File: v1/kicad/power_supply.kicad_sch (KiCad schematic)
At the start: 33 parts, among them J1 Screw_Terminal_01x03, U14 LM7812, U8 LM7815, U9 LM7915

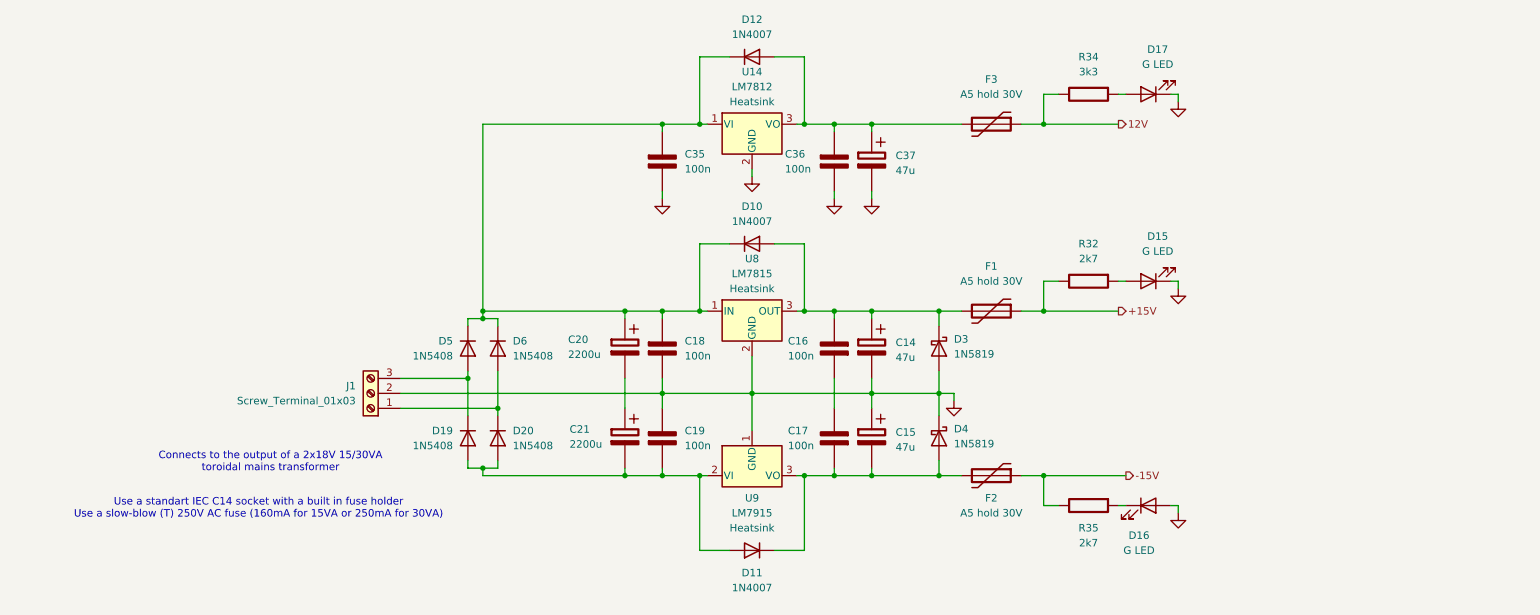
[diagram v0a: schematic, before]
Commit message: Changed the file structure
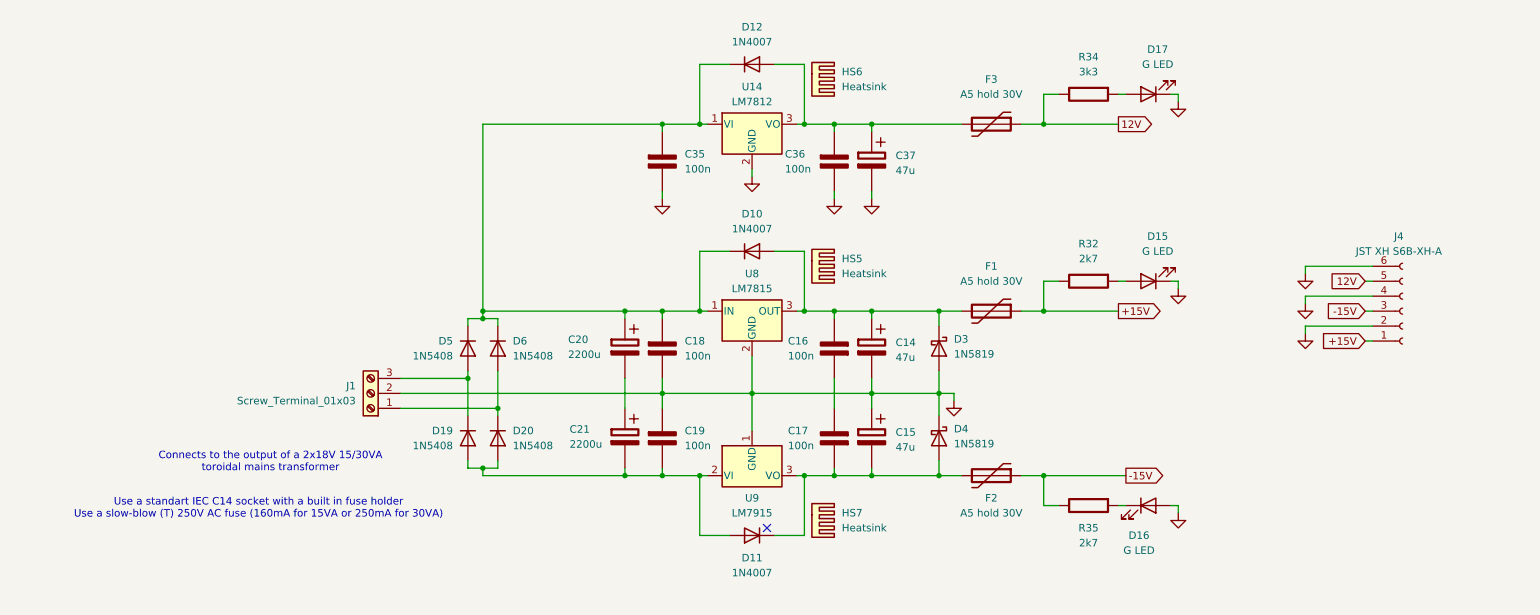
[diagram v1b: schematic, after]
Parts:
- added HS5, HS6, HS7: Heatsink, symbol Mechanical:Heatsink
- added J4: JST XH S6B-XH-A, Connector_JST:JST_XH_S6B-XH-A_1x06_P2.50mm_Horizontal, symbol Connector:Conn_01x06_Socket
- D10, D11, D12: footprint Diode_THT:D_DO-35_SOD27_P7.62mm_Horizontal -> Diode_THT:D_DO-41_SOD81_P10.16mm_Horizontal
- D3, D4: footprint (none) -> Diode_THT:D_DO-41_SOD81_P10.16mm_Horizontal
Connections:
- net +15V: now also J4.1 (Pin_1)
- net -15V: now also J4.3 (Pin_3)
- net 12V: now also J4.5 (Pin_5)
- net GND: now also J4.2 (Pin_2), J4.4 (Pin_4), J4.6 (Pin_6)
- new net: C36., C37., D12.2 (A), F3., U14.3 (VO)
- no-connect marks 0 -> 1
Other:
- moved on the sheet: D10, D11, D12

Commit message: Added a DUT board, changed the output connectors , added test hooks, removed unnecessary switches, added FET support
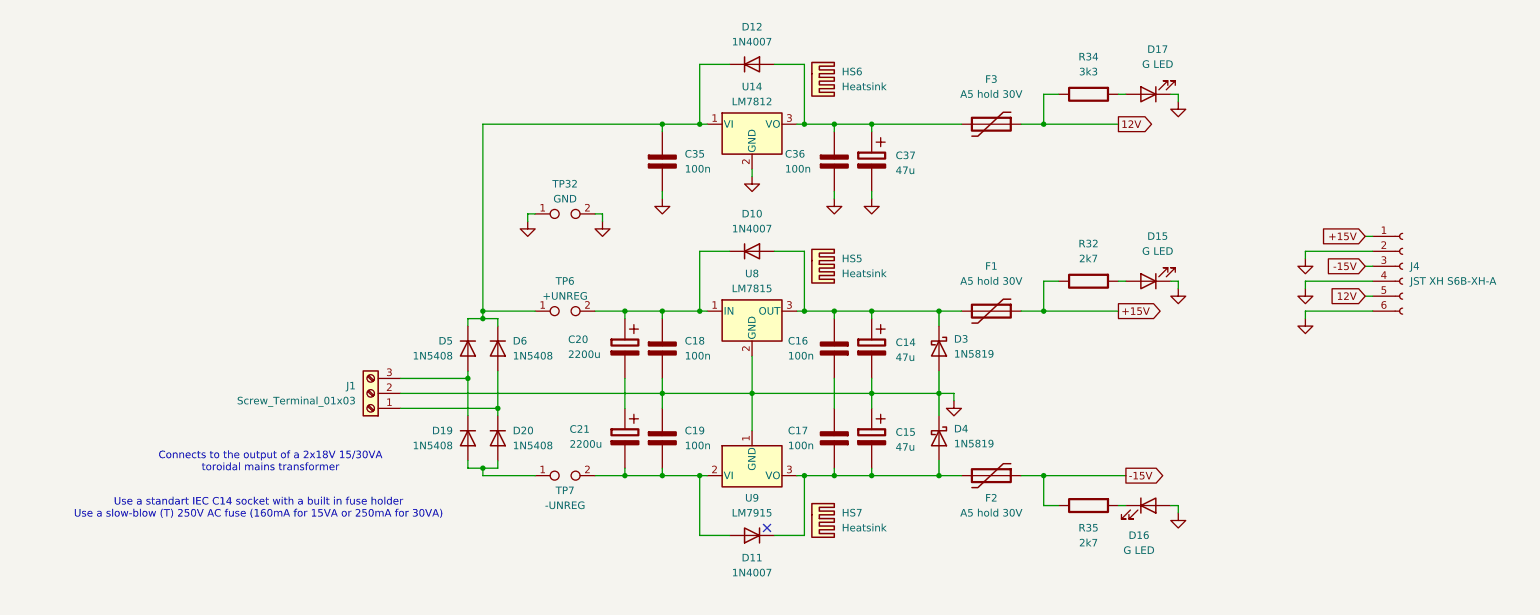
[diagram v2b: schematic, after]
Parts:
- added TP32: GND, symbol Connector:TestPoint_2Pole
- added TP6: +UNREG, symbol Connector:TestPoint_2Pole
- added TP7: -UNREG, symbol Connector:TestPoint_2Pole
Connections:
- net GND: now also TP32.1, TP32.2
- new net: C18., C20., D10.1 (K), TP6.2, U8.1 (IN)
- new net: C19., C21., D11.2 (A), TP7.2, U9.2 (VI)
- new net: D19.2 (A), D20.2 (A), TP7.1
- new net: C36., C37., D12.2 (A), F3., U14.3 (VO)
- new net: C35., D12.1 (K), D5.1 (K), D6.1 (K), TP6.1, U14.1 (VI)
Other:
- moved on the sheet: J4

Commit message: Added power connector
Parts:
- J1: value Screw_Terminal_01x03 -> 1718757
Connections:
- new net: C36., C37., D12.2 (A), F3., U14.3 (VO)
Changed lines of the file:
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@@
 			)
 		)
-		(property "Value" "Screw_Terminal_01x03"
+		(property "Value" "1718757"
 			(at 81.28 100.33 0)
 			(show_name no)

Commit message: Adding KiKit multiboarding
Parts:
- removed J1: 1718757, symbol Connector:Screw_Terminal_01x03
- removed J4: JST XH S6B-XH-A, Connector_JST:JST_XH_S6B-XH-A_1x06_P2.50mm_Horizontal, symbol Connector:Conn_01x06_Socket
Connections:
- net L1: now reaches D19.1 (K), D5.2 (A)
- net L2: now reaches D20.1 (K), D6.2 (A)
- net GND renamed GNDPWR
- new net: C36., C37., D12.2 (A), F3., U14.3 (VO)
- no-connect marks 1 -> 0

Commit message: Fixed mistakes with the polarity of some caps
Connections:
- net GNDPWR: now also C16., C17., C20., C21.
- new net: C36., C37., D12.2 (A), F3., U14.3 (VO)
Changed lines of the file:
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@@
+	)
+	(junction
+		(at 127 99.06)
+		(diameter 0)
+		(color 0 0 0 0)
 	)
 	(junction
@@
 	)
 	(junction
+		(at 162.56 99.06)
+		(diameter 0)
+		(color 0 0 0 0)
+	)
+	(junction
 		(at 168.91 85.09)
 		(diameter 0)
@@
 	(wire
 		(pts
-			(xy 162.56 96.52) (xy 162.56 101.6)
+			(xy 162.56 99.06) (xy 162.56 101.6)
 		)
 		(stroke
@@
 	(wire
 		(pts
+			(xy 127 99.06) (xy 127 101.6)
+		)
+		(stroke
+			(width 0)
+			(type default)
+		)
+	)
+	(wire
+		(pts
 			(xy 168.91 113.03) (xy 180.34 113.03)
 		)
@@
 	(wire
 		(pts
-			(xy 148.59 99.06) (xy 168.91 99.06)
+			(xy 148.59 99.06) (xy 162.56 99.06)
 		)
 		(stroke
@@
 	(wire
 		(pts
+			(xy 127 96.52) (xy 127 99.06)
+		)
+		(stroke
+			(width 0)
+			(type default)
+		)
+	)
+	(wire
+		(pts
 			(xy 102.87 53.34) (xy 102.87 85.09)
 		)
@@
 	(wire
 		(pts
+			(xy 162.56 96.52) (xy 162.56 99.06)
+		)
+		(stroke
+			(width 0)
+			(type default)
+		)
+	)
+	(wire
+		(pts
 			(xy 156.21 113.03) (xy 157.48 113.03)
 		)
@@
 	(wire
 		(pts
+			(xy 127 99.06) (xy 133.35 99.06)
+		)
+		(stroke
+			(width 0)
+			(type default)
+		)
+	)
+	(wire
+		(pts
 			(xy 180.34 99.06) (xy 180.34 102.87)
 		)
@@
 	(wire
 		(pts
-			(xy 127 96.52) (xy 127 101.6)
-		)
-		(stroke
-			(width 0)
-			(type default)
-		)
-	)
-	(wire
-		(pts
 			(xy 152.4 74.93) (xy 157.48 74.93)
 		)
@@
 	(wire
 		(pts
-			(xy 88.9 99.06) (xy 133.35 99.06)
+			(xy 88.9 99.06) (xy 127 99.06)
 		)
 		(stroke
@@
 		)
 		(stroke
+			(width 0)
+			(type default)
+		)
+	)
+	(wire
+		(pts
+			(xy 162.56 99.06) (xy 168.91 99.06)
+		)
+		(stroke

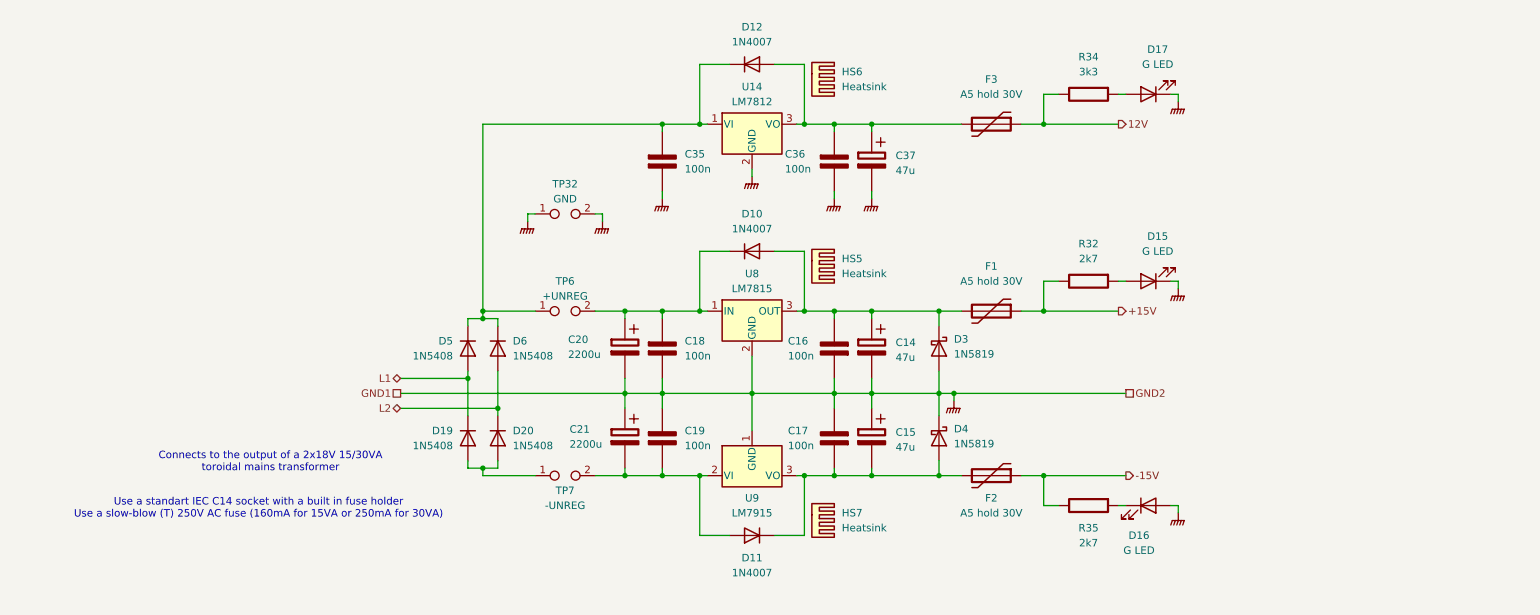
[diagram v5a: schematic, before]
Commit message: Fixed mistakes and made making a BOM easier
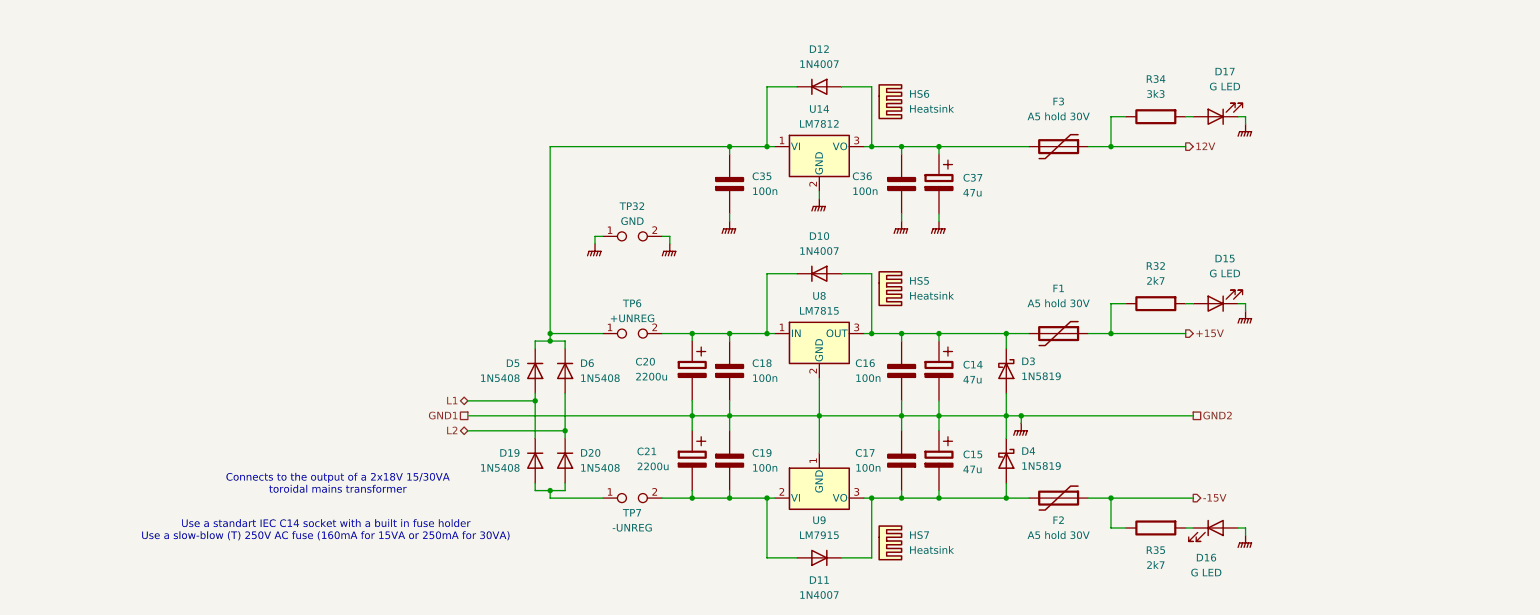
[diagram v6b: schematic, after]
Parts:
- C14, C15, C20, C21, C37: Spend (none) -> $$$
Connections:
- net +15V: now also F1.1, R32.2; no longer F1., R32.
- net -15V: now also F2.1, R35.2; no longer F2., R35.
- net 12V: now also F3.1, R34.2; no longer F3., R34.
- net GNDPWR: now also C14.2, C15.1, C16.1, C17.2, C18.2, C19.1, C20.2, C21.1, C35.2, C36.2, C37.2; no longer C14., C15., C16., C17., C18., C19., C20., C21., C35., C36., C37.
- net at D10.2 (A), D3.1 (K), U8.3 (OUT): now also C14.1, C16.2, F1.2; no longer C14., C16., F1.
- net at D16.1 (K): now also R35.1; no longer R35.
- net at D10.1 (K), TP6.2, U8.1 (IN): now also C18.1, C20.1; no longer C18., C20.
- net at D15.2 (A): now also R32.1; no longer R32.
- net at D11.1 (K), D4.2 (A), U9.3 (VO): now also C15.2, C17.1, F2.2; no longer C15., C17., F2.
- net at D11.2 (A), TP7.2, U9.2 (VI): now also C19.2, C21.2; no longer C19., C21.
- net at D12.1 (K), D5.1 (K), D6.1 (K)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: now also C35.1; no longer C35.
- net at D17.2 (A): now also R34.1; no longer R34.
- new net: C36.1, C37.1, D12.2 (A), F3.2, U14.3 (VO)
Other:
- moved on the sheet: C14, C15, C16, C17, C18, C19, C20, C21, C35, C36, C37, D10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
